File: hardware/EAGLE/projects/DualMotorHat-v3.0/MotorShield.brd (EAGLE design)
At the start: 100 x 80 mm, 86 parts, among them IC2_0_PC JP, U0-C1 0.1uF, U0-C2 1nF, U0-C3 0.22uF, U0-C4 0.1uF, U0-C5 0.22uF, U0-R1 4.7k, U0-R2 47k, U0-R3 10k, U0-R4 10k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

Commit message: motorhad finished
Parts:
- moved V1-C1 7.62 mm to (35.6, 25.4), turned to 180 degrees
- moved V1-C5 7.62 mm to (35.6, 33.0), turned to 180 degrees
- moved V1-R1 7.62 mm to (40.0, 25.4), turned to 180 degrees
- moved V1-R4 7.62 mm to (44.5, 25.4), turned to 180 degrees
- moved W1-C1 7.62 mm to (35.6, 36.8), turned to 180 degrees
- moved W1-C5 7.62 mm to (35.6, 44.5), turned to 180 degrees
- moved W1-R1 7.62 mm to (40.0, 36.8), turned to 180 degrees
- moved W1-R4 7.62 mm to (44.5, 36.8), turned to 180 degrees
- moved U1-C1 6.75 mm to (35.6, 14.0)
- moved U1-C2 6.75 mm to (40.0, 19.1)
- moved SERVO_0 3.81 mm to (8.89, 7.62)
- moved SERVOS 3.59 mm to (11.4, 11.4)
- moved V1-C2 2.54 mm to (40.0, 30.5), turned to 180 degrees
- moved V1-C3 2.54 mm to (35.6, 27.9), turned to 180 degrees
- moved V1-C4 2.54 mm to (35.6, 30.5), turned to 180 degrees
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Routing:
- net 3.3V: track 0.00 -> 173.8 mm, vias 0 -> 4
- net GND: track 222.0 -> 391.6 mm, vias 6 -> 11
- net SPI_MOSI: track 0.00 -> 73.6 mm, vias 0 -> 1
- net SPI_MISO: track 0.00 -> 71.7 mm, vias 0 -> 2
- net SPI_SCLK: track 0.00 -> 63.9 mm, vias 0 -> 3
- net U1: track 0.00 -> 52.0 mm, vias 0 -> 1
- net VI: track 222.3 -> 273.8 mm, vias 3 -> 6
- net W1: track 0.00 -> 50.6 mm, vias 0 -> 1
- net IS_W1: track 0.00 -> 47.9 mm, vias 0 -> 2
- net V1: track 0.00 -> 44.3 mm, vias 0 -> 1
- net SPI_CS0: track 0.00 -> 38.8 mm, vias 0 -> 1
- net IN_U1: track 0.00 -> 38.1 mm, vias 0 -> 2
- net IS_V1: track 0.00 -> 37.9 mm, vias 0 -> 2
- net SPI_CS1: track 0.00 -> 35.9 mm, vias 0 -> 1
- net IN_U0: track 0.00 -> 30.4 mm, vias 0 -> 3
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
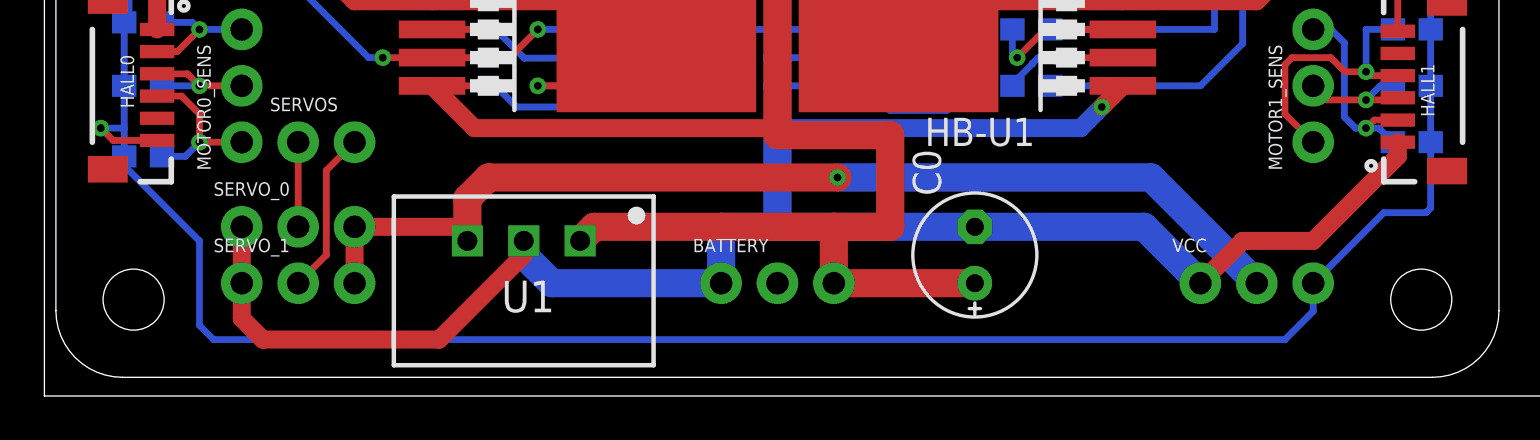
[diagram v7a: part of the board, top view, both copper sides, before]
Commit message: vcc jumper update
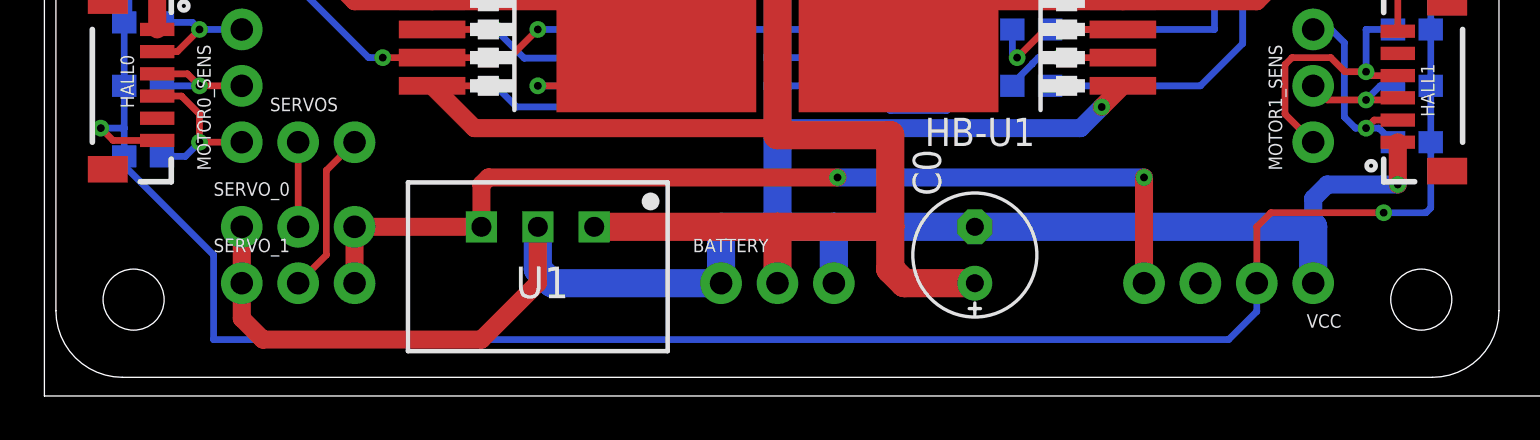
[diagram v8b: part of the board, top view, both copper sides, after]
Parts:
- VCC: value (none) -> JP; device SparkFun-Connectors:1X03_NO_SILK -> SparkFun-Connectors:1X04_NO_SILK
- moved VCC 5.08 mm to (57.1, 5.08), turned to 180 degrees
- moved U1 0.90 mm to (22.2, 7.62)
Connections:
- new net VCC-SERVOS: SERVO_0.3, SERVO_1.3, U1.3, VCC.4
- net 3.3V: now also VCC.2; no longer VCC.3
- net 5.0V: now also VCC.3; no longer SERVO_0.3, SERVO_1.3, U1.3, VCC.2
- net GND: now also BATTERY.3
- net VI: now also BATTERY.2; no longer BATTERY.3
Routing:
- net 5.0V: track 47.5 -> 0.00 mm, vias 1 -> 0
- net VCC-SERVOS: track 0.00 -> 44.9 mm, vias 0 -> 2
- net GND: track 391.6 -> 401.0 mm, vias 11 -> 12
- net 3.3V: track 173.8 -> 175.3 mm, vias 4 -> 5
- net VI: track 273.8 -> 272.6 mm
